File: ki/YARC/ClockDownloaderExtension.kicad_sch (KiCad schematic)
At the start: 19 parts, among them J4 NANOIO_EXT, J5 MCR_EXT, J6 PULSE_EXT, J7 CONTROLS, U10 74HC74, U11 74HCT574, U12 74HC14, U13 74LS32, U15 74LS08, U16 74LS138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

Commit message: Ongoing development
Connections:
- net ~{SET_SERVICE}: now also U16.15 (O0); no longer U16.7 (O7)
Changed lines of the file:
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@@
+    (stroke (width 0) (type default) (color 0 0 0 0))
+  )
+  (wire (pts (xy 187.96 111.76) (xy 193.04 111.76))
     (stroke (width 0) (type default) (color 0 0 0 0))
   )
@@
   )
   (bus (pts (xy 73.66 137.16) (xy 76.2 137.16))
-    (stroke (width 0) (type default) (color 0 0 0 0))
-  )
-  (wire (pts (xy 187.96 129.54) (xy 193.04 129.54))
     (stroke (width 0) (type default) (color 0 0 0 0))
   )
@@
     (stroke (width 0) (type default) (color 0 0 0 0))
   )
-  (wire (pts (xy 193.04 86.36) (xy 193.04 129.54))
+  (wire (pts (xy 193.04 86.36) (xy 193.04 111.76))
     (stroke (width 0) (type default) (color 0 0 0 0))
   )

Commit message: Flags development and implement memory fix. Firmware not updated to match the memory fix.
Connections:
- net ~{MCR_BIT_7_REG_WR_EN_L}: now reaches J5.4 (Pin_4)
- net ~{HIGH_UNUSED_OFFBOARD_3}: now reaches J6.1 (Pin_1)
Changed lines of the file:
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@@
+    )
+  )
+  (global_label "~{HIGH_UNUSED_OFFBOARD_3}" (shape input) (at 127 149.86 90) (fields_autoplaced)
+    (effects (font (size 1.27 1.27)) (justify left))
+    (property "Intersheet References" "${INTERSHEET_REFS}" (id 0) (at 126.9206 121.4421 90)
+      (effects (font (size 1.27 1.27)) (justify left) hide)
     )
   )
@@
       (effects (font (size 1.27 1.27)) (justify left) hide)
     )
+  )
+  (global_label "~{MCR_BIT_7_REG_WR_EN_L}" (shape input) (at 114.3 149.86 90) (fields_autoplaced)
+    (effects (font (size 1.27 1.27)) (justify left))
+    (property "Intersheet References" "${INTERSHEET_REFS}" (id 0) (at 114.2206 123.6798 90)
+      (effects (font (size 1.27 1.27)) (justify left) hide)
+    )

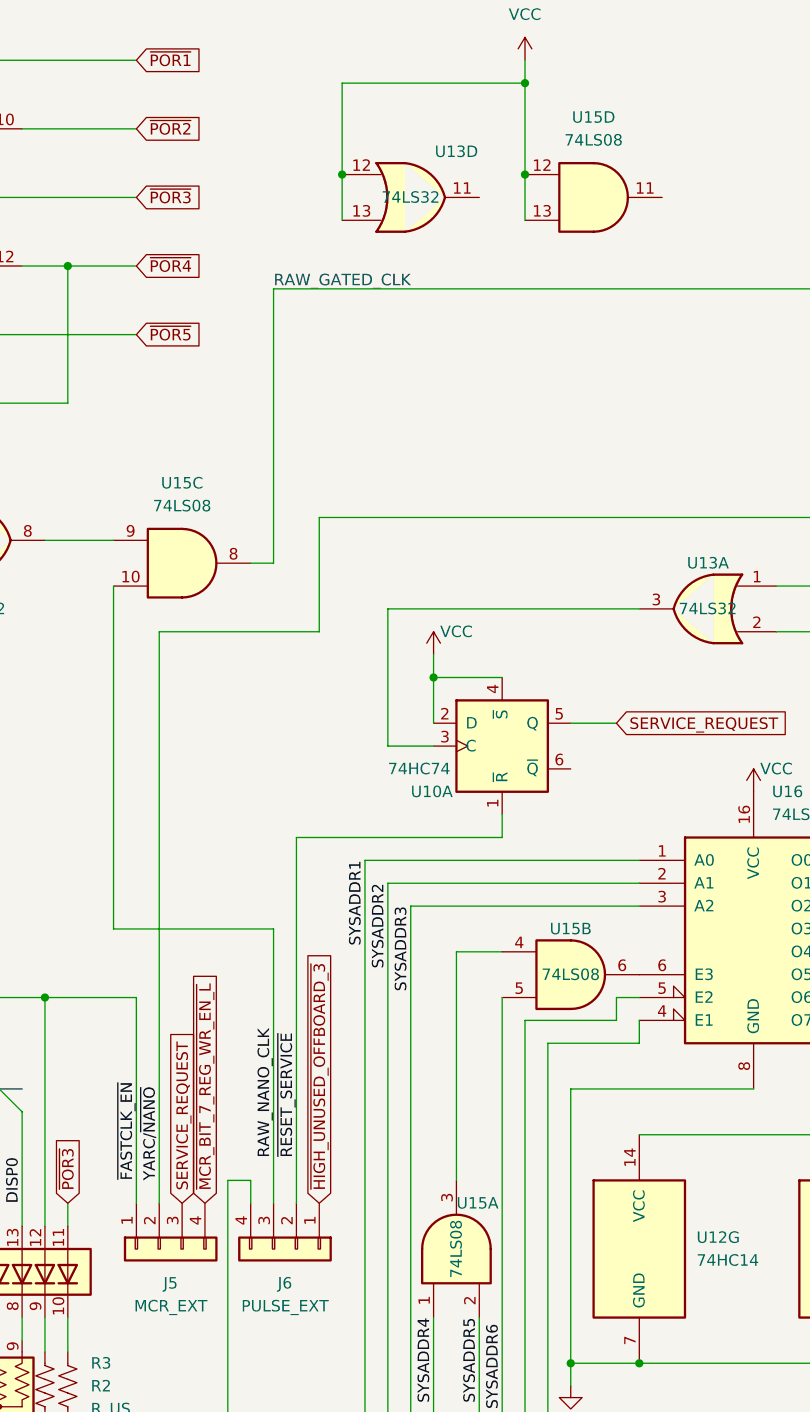
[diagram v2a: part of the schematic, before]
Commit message: Convert schematic to KiCad 7
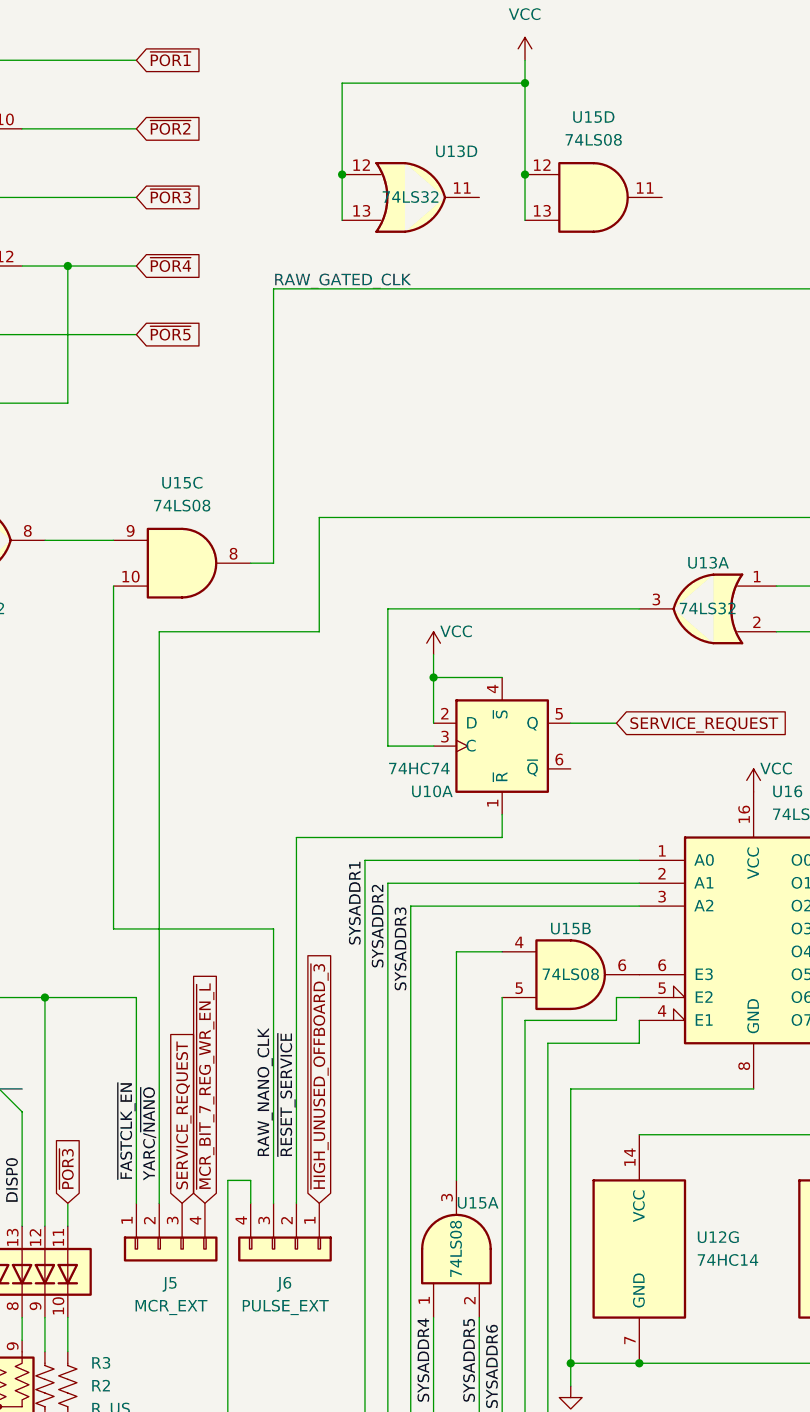
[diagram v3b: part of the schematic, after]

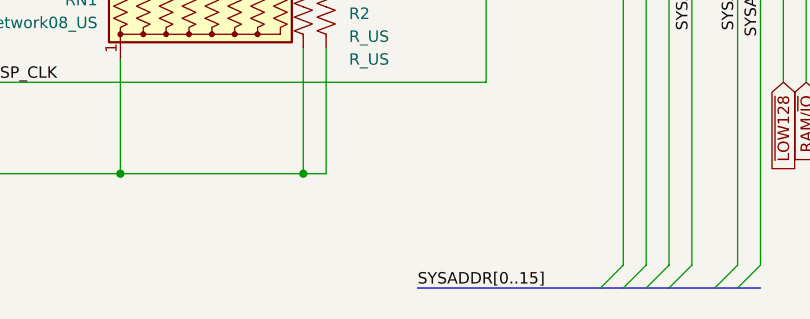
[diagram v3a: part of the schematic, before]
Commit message: Removed about 2/3 of 2300+ errors from the ERC
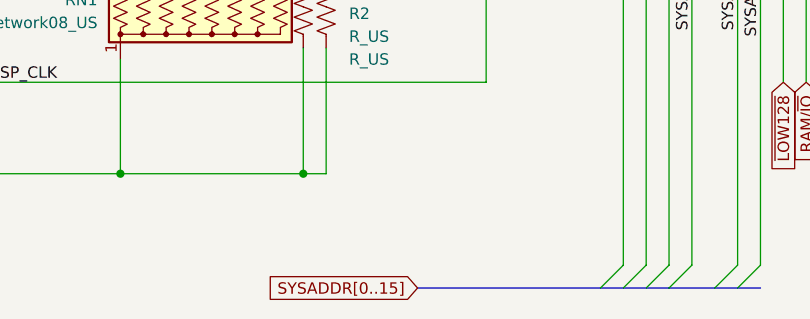
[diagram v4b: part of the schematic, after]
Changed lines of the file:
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@@
-    (effects (font (size 1.27 1.27)) (justify left bottom))
-  )
-  (label "SYSADDR[0..15]" (at 109.22 200.66 0) (fields_autoplaced)
     (effects (font (size 1.27 1.27)) (justify left bottom))
   )
@@
     )
   )
+  (global_label "SYSADDR[0..15]" (shape input) (at 109.22 200.66 180) (fields_autoplaced)
+    (effects (font (size 1.27 1.27)) (justify right))
+    (property "Intersheetrefs" "${INTERSHEET_REFS}" (at 91.2971 200.66 0)
+      (effects (font (size 1.27 1.27)) (justify right) hide)
+    )
+  )

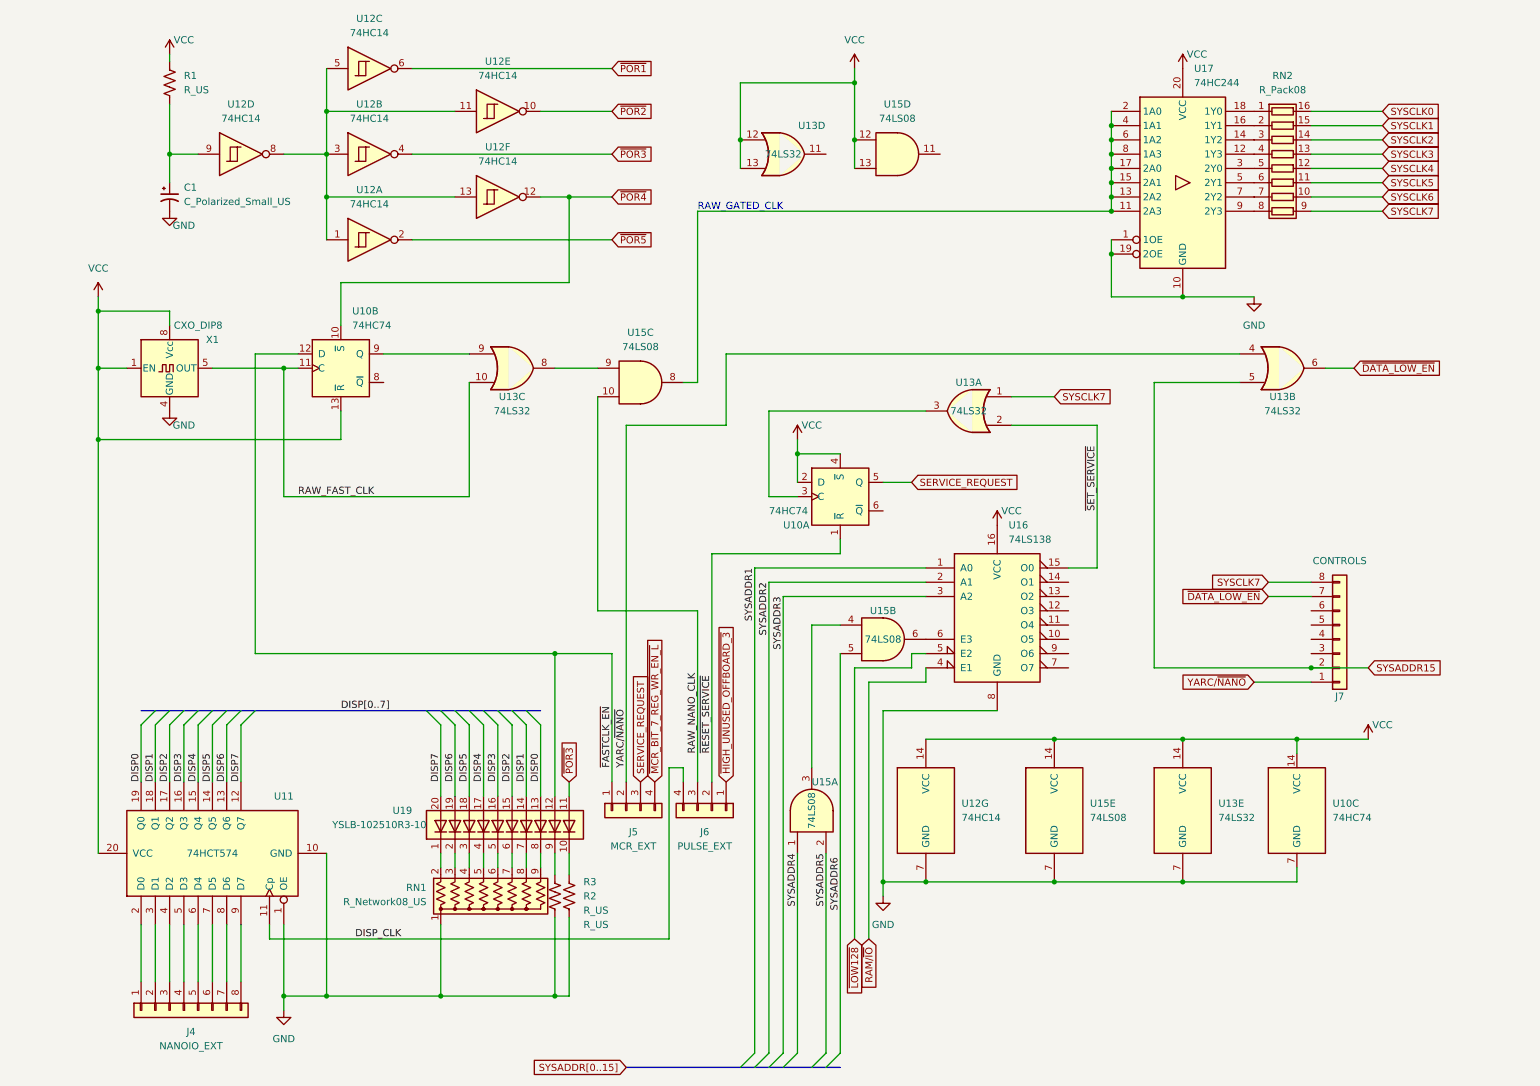
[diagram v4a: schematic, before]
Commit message: Ongoing fixes for ERC errors
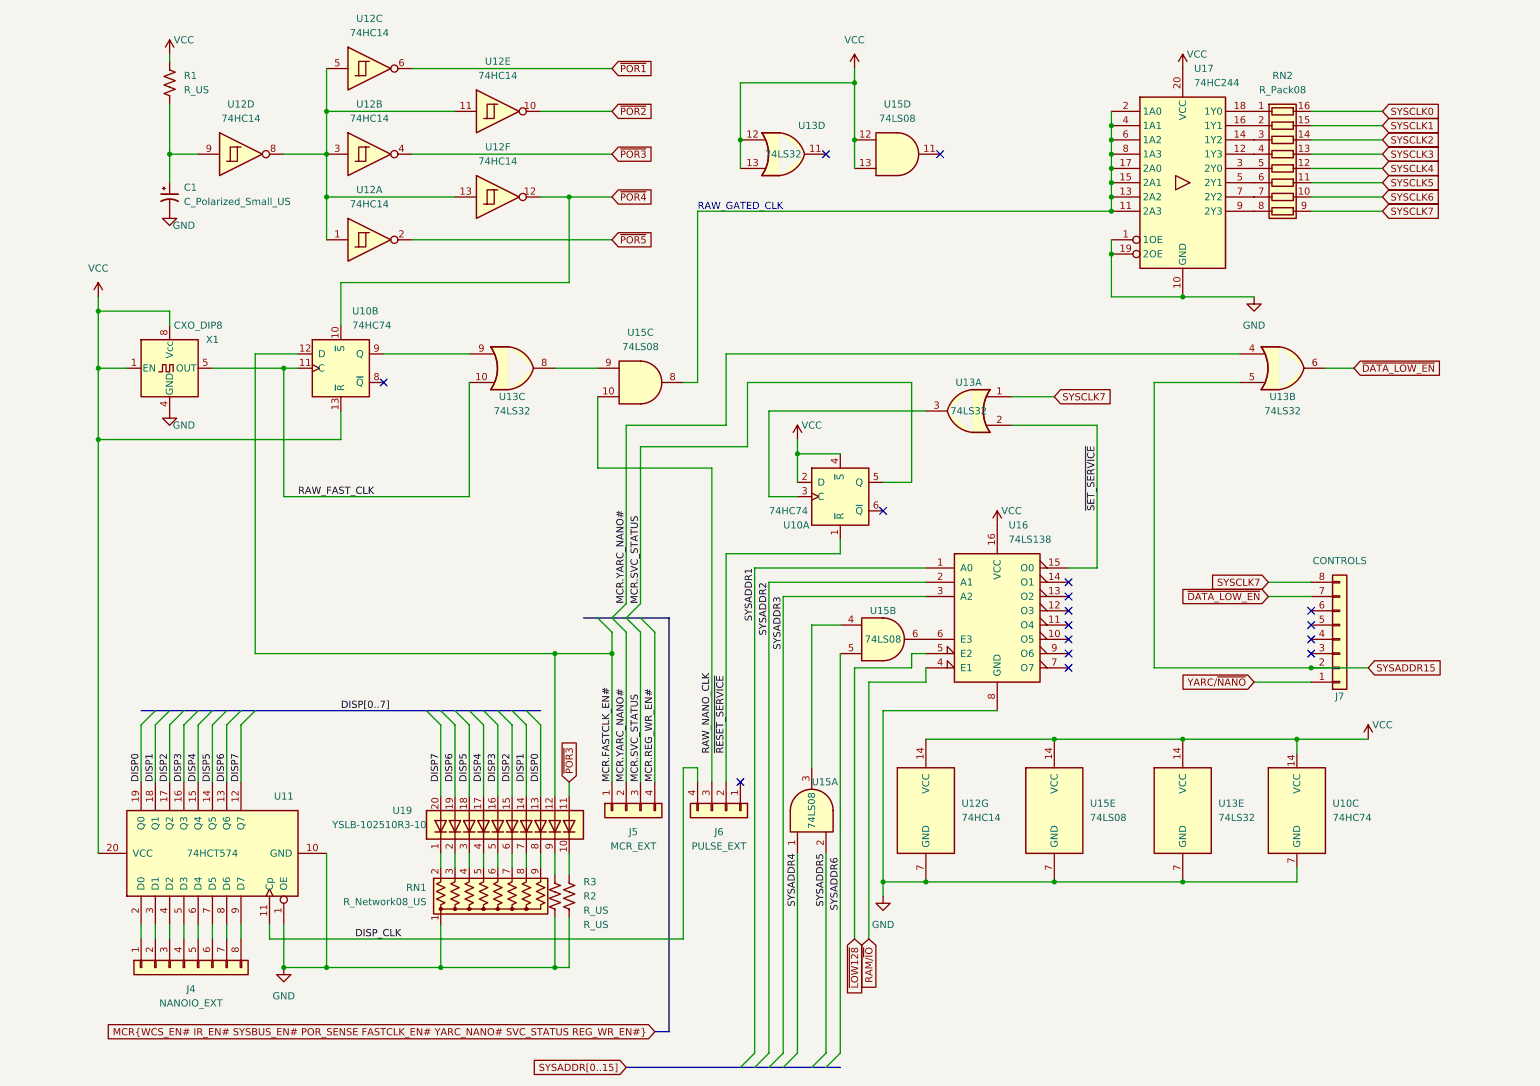
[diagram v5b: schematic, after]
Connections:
- net YARC/~{NANO}: no longer J5.2 (Pin_2), U13.4
- net SERVICE_REQUEST renamed MCR.SVC_STATUS
- net ~{FASTCLK_EN} renamed MCR.FASTCLK_EN#
- net ~{HIGH_UNUSED_OFFBOARD_3}: no longer names the net of J6.1 (Pin_1)
- net ~{MCR_BIT_7_REG_WR_EN_L} renamed MCR.REG_WR_EN#
- new net MCR.YARC_NANO#: J5.2 (Pin_2), U13.4
- no-connect marks 0 -> 16
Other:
- moved on the sheet: J4, J6

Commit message: Continuing cleanup of schematic
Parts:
- removed J4: NANOIO_EXT, symbol Connector_Generic:Conn_01x08
- removed J5: MCR_EXT, symbol Connector_Generic:Conn_01x04
- removed J6: PULSE_EXT, symbol Connector_Generic:Conn_01x04
- removed J7: CONTROLS, symbol Connector_Generic:Conn_01x08
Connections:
- net NANOIO0: now reaches U11.2 (D0)
- net NANOIO1: now reaches U11.3 (D1)
- net NANOIO2: now reaches U11.4 (D2)
- net NANOIO3: now reaches U11.5 (D3)
- net NANOIO4: now reaches U11.6 (D4)
- net NANOIO5: now reaches U11.7 (D5)
- net NANOIO6: now reaches U11.8 (D6)
- net NANOIO7: now reaches U11.9 (D7)
- net SYSCLK0: no longer names the net of RN2.16 (R1.2)
- net SYSCLK1: no longer names the net of RN2.15 (R2.2)
- net SYSCLK2: no longer names the net of RN2.14 (R3.2)
- net SYSCLK3: no longer names the net of RN2.13 (R4.2)
- net SYSCLK4: no longer names the net of RN2.12 (R5.2)
- net SYSCLK5: no longer names the net of RN2.11 (R6.2)
- net SYSCLK6: no longer names the net of RN2.10 (R7.2)
- net SYSCLK7 renamed SYSCLK
- net ~{POR1}: no longer names the net of U12.6
- net ~{POR2}: no longer names the net of U12.10
- net ~{RESET_SERVICE} renamed RESET_SERVICE
- no-connect marks 16 -> 20
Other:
- note added: "In reality, there is some fanout from the various buffers. But I just called them all SYSCLK."
